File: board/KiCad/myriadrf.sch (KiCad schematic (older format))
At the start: 1 part, among them J1 FX10B_80S_8

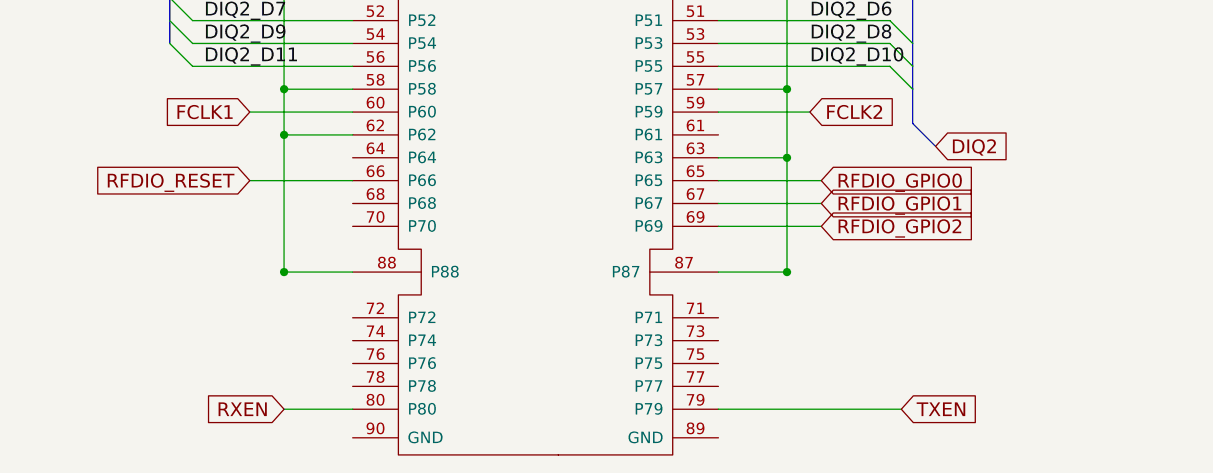
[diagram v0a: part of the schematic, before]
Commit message: control signals added
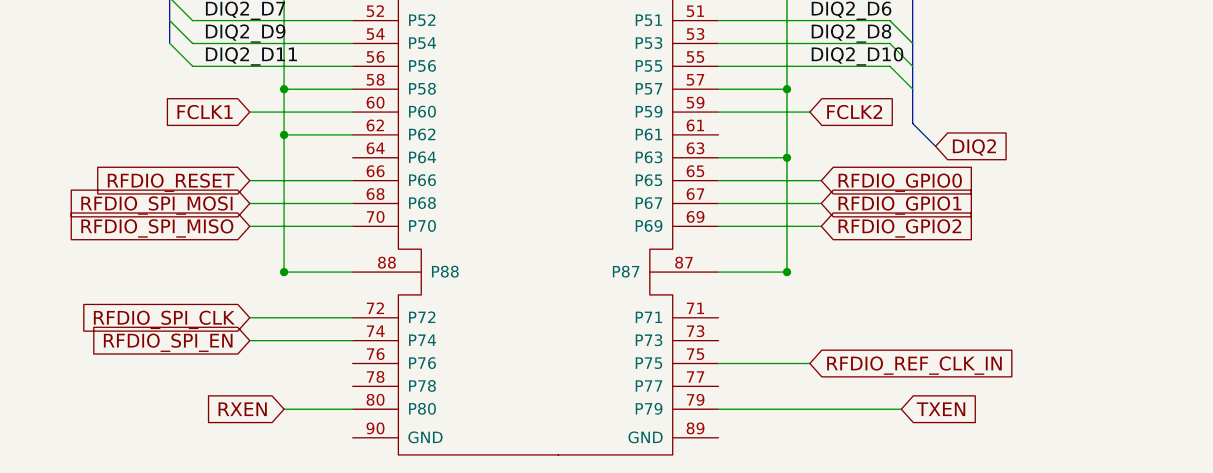
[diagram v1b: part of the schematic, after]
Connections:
- net RFDIO_SPI_MOSI: now reaches J1.68 (P68)
- net RFDIO_SPI_MISO: now reaches J1.70 (P70)
- net RFDIO_SPI_CLK: now reaches J1.72 (P72)
- net RFDIO_SPI_EN: now reaches J1.74 (P74)
- net RFDIO_REF_CLK_IN: now reaches J1.75 (P75)
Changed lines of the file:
@@
 Text GLabel 4350 5350 0    60   Input ~ 0
 RFDIO_RESET
+Wire Wire Line
+	4800 5450 4350 5450
+Text GLabel 4350 5450 0    60   Input ~ 0
+RFDIO_SPI_MOSI
+Wire Wire Line
+	4800 5550 4350 5550
+Text GLabel 4350 5550 0    60   Input ~ 0
+RFDIO_SPI_MISO
+Wire Wire Line
+	4800 5950 4350 5950
+Text GLabel 4350 5950 0    60   Input ~ 0
+RFDIO_SPI_CLK
+Wire Wire Line
+	4800 6050 4350 6050
+Text GLabel 4350 6050 0    60   Input ~ 0
+RFDIO_SPI_EN
+Wire Wire Line
+	6400 6150 6800 6150
+Text GLabel 6800 6150 2    60   Input ~ 0
+RFDIO_REF_CLK_IN
 $EndSCHEMATC

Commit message: Finalize first draft
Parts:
- J1: footprint (none) -> pmod:FX10B_80S_8
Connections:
- net GND: now also J1.89 (GND), J1.90 (GND)
- no-connect marks 0 -> 21
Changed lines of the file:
@@
 F 0 "J1" H 5600 6687 60  0000 C CNN
 F 1 "FX10B_80S_8" H 5580 6720 60  0001 C CNN
-F 2 "" H 5590 6840 60  0001 C CNN
+F 2 "pmod:FX10B_80S_8" H 5590 6840 60  0001 C CNN
 F 3 "" H 5600 3750 60  0000 C CNN
 F 4 "CONN RECEPT, 80POS, W/O, POST, SMD," H 5630 6950 60  0001 C CNN "Description"
@@
 5V
 $Comp
-L GND #PWR12
+L GND #PWR13
 U 1 1 56AB8EA2
 P 4400 1450
-F 0 "#PWR12" H 4400 1200 50  0001 C CNN
+F 0 "#PWR13" H 4400 1200 50  0001 C CNN
 F 1 "GND" H 4400 1300 50  0000 C CNN
 F 2 "" H 4400 1450 60  0000 C CNN
@@
 $EndComp
 $Comp
-L GND #PWR13
+L GND #PWR28
 U 1 1 56AB8EB8
 P 7350 1450
-F 0 "#PWR13" H 7350 1200 50  0001 C CNN
+F 0 "#PWR28" H 7350 1200 50  0001 C CNN
 F 1 "GND" H 7350 1300 50  0000 C CNN
 F 2 "" H 7350 1450 60  0000 C CNN
@@
 	1    0    0    -1
 $EndComp
-Entry Wire Line
-	7150 2650 7250 2750
-Entry Wire Line
-	7150 2750 7250 2850
-Entry Wire Line
-	7150 2950 7250 3050
-Entry Wire Line
-	7150 3350 7250 3450
-Entry Wire Line
-	7150 3450 7250 3550
-Entry Wire Line
-	7150 3550 7250 3650
 Wire Wire Line
 	6400 1250 7250 1250
@@
 Wire Wire Line
 	4800 3550 4100 3550
-Wire Bus Line
-	7250 2750 7250 3800
-Entry Wire Line
-	4000 2550 4100 2650
-Entry Wire Line
-	4000 2650 4100 2750
-Entry Wire Line
-	4000 2850 4100 2950
-Entry Wire Line
-	4000 3250 4100 3350
-Entry Wire Line
-	4000 3350 4100 3450
-Entry Wire Line
-	4000 3450 4100 3550
-Wire Bus Line
-	4000 3450 4000 2400
-Text Label 6800 2650 0    60   ~ 0
-DIQ1_D0
-Text Label 6800 2750 0    60   ~ 0
-DIQ1_D2
-Text Label 6800 2950 0    60   ~ 0
-DIQ1_D4
-Text Label 6800 3350 0    60   ~ 0
-DIQ1_D6
-Text Label 6800 3450 0    60   ~ 0
-DIQ1_D8
-Text Label 6800 3550 0    60   ~ 0
-DIQ1_D10
-Text Label 4150 2650 0    60   ~ 0
-DIQ1_D1
-Text Label 4150 2750 0    60   ~ 0
-DIQ1_D3
-Text Label 4150 2950 0    60   ~ 0
-DIQ1_D5
-Text Label 4150 3350 0    60   ~ 0
-DIQ1_D7
-Text Label 4150 3450 0    60   ~ 0
-DIQ1_D9
-Text Label 4150 3550 0    60   ~ 0
-DIQ1_D11
-Text GLabel 7350 3900 2    60   Input ~ 0
-DIQ1
-Text GLabel 3900 2300 0    60   Input ~ 0
-DIQ1
-Entry Bus Bus
-	7250 3800 7350 3900
-Entry Bus Bus
-	3900 2300 4000 2400
 Wire Wire Line
 	6400 2450 7150 2450
@@
 Text GLabel 7200 6350 2    60   Input ~ 0
 TXEN
-Wire Bus Line
-	7250 4050 7250 5100
 Wire Wire Line
 	6400 3950 7150 3950
-Entry Wire Line
-	7150 3950 7250 4050
-Entry Wire Line
-	7150 4050 7250 4150
-Entry Wire Line
-	7150 4250 7250 4350
 Wire Wire Line
 	6400 4050 7150 4050
@@
 Wire Wire Line
 	6400 4850 7150 4850
-Entry Wire Line
-	7150 4650 7250 4750
-Entry Wire Line
-	7150 4750 7250 4850
-Entry Wire Line
-	7150 4850 7250 4950
-Text Label 6800 3950 0    60   ~ 0
-DIQ2_D0
-Text Label 6800 4050 0    60   ~ 0
-DIQ2_D2
-Text Label 6800 4250 0    60   ~ 0
-DIQ2_D4
-Text Label 6800 4650 0    60   ~ 0
-DIQ2_D6
-Text Label 6800 4750 0    60   ~ 0
-DIQ2_D8
-Text Label 6800 4850 0    60   ~ 0
-DIQ2_D10
-Entry Bus Bus
-	7250 5100 7350 5200
-Text GLabel 7350 5200 2    60   Input ~ 0
-DIQ2
 Wire Wire Line
 	4800 3950 4100 3950
@@
 Wire Wire Line
 	4800 4850 4100 4850
-Entry Wire Line
-	4000 3850 4100 3950
-Entry Wire Line
-	4000 3950 4100 4050
-Entry Wire Line
-	4000 4150 4100 4250
-Entry Wire Line
-	4000 4550 4100 4650
-Entry Wire Line
-	4000 4650 4100 4750
-Entry Wire Line
-	4000 4750 4100 4850
-Wire Bus Line
-	4000 4750 4000 3850
-Entry Bus Bus
-	3900 3750 4000 3850
-Text GLabel 3900 3750 0    60   Input ~ 0
-DIQ2
-Text Label 4150 3950 0    60   ~ 0
-DIQ2_D1
-Text Label 4150 4050 0    60   ~ 0
-DIQ2_D3
-Text Label 4150 4250 0    60   ~ 0
-DIQ2_D5
-Text Label 4150 4650 0    60   ~ 0
-DIQ2_D7
-Text Label 4150 4750 0    60   ~ 0
-DIQ2_D9
-Text Label 4150 4850 0    60   ~ 0
-DIQ2_D11
 Wire Wire Line
 	6400 5050 6800 5050
@@
 Text GLabel 6800 6150 2    60   Input ~ 0
 RFDIO_REF_CLK_IN
+Text GLabel 4100 2650 0    60   Input ~ 0
+DIQ1_D1
+Text GLabel 4100 2750 0    60   Input ~ 0
+DIQ1_D3
+Text GLabel 4100 2950 0    60   Input ~ 0
+DIQ1_D5
+Text GLabel 4100 3350 0    60   Input ~ 0
+DIQ1_D7
+Text GLabel 4100 3450 0    60   Input ~ 0
+DIQ1_D9
+Text GLabel 4100 3550 0    60   Input ~ 0
+DIQ1_D11
+Text GLabel 7150 2650 2    60   Input ~ 0
+DIQ1_D0
+Text GLabel 7150 2750 2    60   Input ~ 0
+DIQ1_D2
+Text GLabel 7150 2950 2    60   Input ~ 0
+DIQ1_D4
+Text GLabel 7150 3350 2    60   Input ~ 0
+DIQ1_D6
+Text GLabel 7150 3450 2    60   Input ~ 0
+DIQ1_D8
+Text GLabel 7150 3550 2    60   Input ~ 0
+DIQ1_D10
+Text GLabel 7150 3950 2    60   Input ~ 0
+DIQ2_D0
+Text GLabel 7150 4050 2    60   Input ~ 0
+DIQ2_D2
+Text GLabel 7150 4250 2    60   Input ~ 0
+DIQ2_D4
+Text GLabel 7150 4650 2    60   Input ~ 0
+DIQ2_D6
+Text GLabel 7150 4750 2    60   Input ~ 0
+DIQ2_D8
+Text GLabel 7150 4850 2    60   Input ~ 0
+DIQ2_D10
+Text GLabel 4100 3950 0    60   Input ~ 0
+DIQ2_D1
+Text GLabel 4100 4050 0    60   Input ~ 0
+DIQ2_D3
+Text GLabel 4100 4250 0    60   Input ~ 0
+DIQ2_D5
+Text GLabel 4100 4650 0    60   Input ~ 0
+DIQ2_D7
+Text GLabel 4100 4750 0    60   Input ~ 0
+DIQ2_D9
+Text GLabel 4100 4850 0    60   Input ~ 0
+DIQ2_D11
+NoConn ~ 6400 2150
+NoConn ~ 6400 2250
+NoConn ~ 6400 2550
+NoConn ~ 6400 1650
+NoConn ~ 6400 1550
+NoConn ~ 4800 1650
+NoConn ~ 4800 1550
+NoConn ~ 4800 2150
+NoConn ~ 4800 2250
+NoConn ~ 4800 2450
+NoConn ~ 4800 2550
+NoConn ~ 4800 3750
+NoConn ~ 4800 3850
+NoConn ~ 4800 5250
+NoConn ~ 4800 6150
+NoConn ~ 4800 6250
+NoConn ~ 6400 6250
+NoConn ~ 6400 6050
+NoConn ~ 6400 5950
+NoConn ~ 6400 5150
+NoConn ~ 6400 3850
+Wire Wire Line
+	4775 6475 4800 6475
+Wire Wire Line
+	4775 6475 4775 6650
+Wire Wire Line
+	4775 6650 6425 6650
+Wire Wire Line
+	6425 6650 6425 6475
+Wire Wire Line
+	6425 6475 6400 6475
+$Comp
+L GND #PWR23
+U 1 1 56C33F19
+P 5600 6700
+F 0 "#PWR23" H 5600 6450 50  0001 C CNN
+F 1 "GND" H 5608 6526 50  0000 C CNN
+F 2 "" H 5600 6700 50  0000 C CNN
+F 3 "" H 5600 6700 50  0000 C CNN
+	1    5600 6700
+	1    0    0    -1
+$EndComp
+Wire Wire Line
+	5600 6700 5600 6650
+Connection ~ 5600 6650
 $EndSCHEMATC

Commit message: Improve design
* PMOS on input voltage for polarity
* Re-design board to add mount holes and better routing
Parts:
- added P3, P4: Myriad_Mount_Hole, pmod:Myriad_Mount_Hole, symbol Myriad_Mount_Hole
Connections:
- wire segments 77 -> 80
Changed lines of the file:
@@
 5V
 $Comp
-L GND #PWR13
+L GND #PWR26
 U 1 1 56AB8EA2
 P 4400 1450
-F 0 "#PWR13" H 4400 1200 50  0001 C CNN
+F 0 "#PWR26" H 4400 1200 50  0001 C CNN
 F 1 "GND" H 4400 1300 50  0000 C CNN
 F 2 "" H 4400 1450 60  0000 C CNN
@@
 Connection ~ 6700 2050
 Connection ~ 6700 1850
-Connection ~ 7150 1250
 Wire Wire Line
 	6400 2350 6700 2350
@@
 	6425 6475 6400 6475
 $Comp
-L GND #PWR23
+L GND #PWR27
 U 1 1 56C33F19
 P 5600 6700
-F 0 "#PWR23" H 5600 6450 50  0001 C CNN
+F 0 "#PWR27" H 5600 6450 50  0001 C CNN
 F 1 "GND" H 5608 6526 50  0000 C CNN
 F 2 "" H 5600 6700 50  0000 C CNN
@@
 	5600 6700 5600 6650
 Connection ~ 5600 6650
+$Comp
+L Myriad_Mount_Hole P3
+U 1 1 56C31CE7
+P 9550 1300
+F 0 "P3" H 9684 1353 60  0000 L CNN
+F 1 "Myriad_Mount_Hole" H 9684 1247 60  0000 L CNN
+F 2 "pmod:Myriad_Mount_Hole" H 9550 1300 60  0001 C CNN
+F 3 "" H 9550 1300 60  0000 C CNN
+	1    9550 1300
+	1    0    0    -1
+$EndComp
+$Comp
+L Myriad_Mount_Hole P4
+U 1 1 56C31DC9
+P 9550 1575
+F 0 "P4" H 9684 1628 60  0000 L CNN
+F 1 "Myriad_Mount_Hole" H 9684 1522 60  0000 L CNN
+F 2 "pmod:Myriad_Mount_Hole" H 9550 1575 60  0001 C CNN
+F 3 "" H 9550 1575 60  0000 C CNN
+	1    9550 1575
+	1    0    0    -1
+$EndComp
+Wire Wire Line
+	9125 1300 9125 1675
+Wire Wire Line
+	9125 1300 9250 1300
+Wire Wire Line
+	9250 1575 9125 1575
+Connection ~ 9125 1575
+$Comp
+L GND #PWR29
+U 1 1 56C3306B
+P 9125 1675
+F 0 "#PWR29" H 9125 1425 50  0001 C CNN
+F 1 "GND" H 9125 1525 50  0000 C CNN
+F 2 "" H 9125 1675 60  0000 C CNN
+F 3 "" H 9125 1675 60  0000 C CNN
+	1    9125 1675
+	1    0    0    -1
+$EndComp
 $EndSCHEMATC

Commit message: Housekeeping
Structure libraries and put proper licenses to them.
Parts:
- J1: footprint pmod:FX10B_80S_8 -> MyriadRF:FX10B_80S_8
- P3, P4: footprint pmod:Myriad_Mount_Hole -> lms6002-pmod:Myriad_Mount_Hole
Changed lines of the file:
@@
 LIBS:contrib
 LIBS:valves
+LIBS:lms6002-pmod
 LIBS:ice40_1k4k_tq144
 LIBS:myriad
-LIBS:pmod
-LIBS:LMS6002-Pmod-cache
 EELAYER 25 0
 EELAYER END
@@
 F 0 "J1" H 5600 6687 60  0000 C CNN
 F 1 "FX10B_80S_8" H 5580 6720 60  0001 C CNN
-F 2 "pmod:FX10B_80S_8" H 5590 6840 60  0001 C CNN
+F 2 "MyriadRF:FX10B_80S_8" H 5590 6840 60  0001 C CNN
 F 3 "" H 5600 3750 60  0000 C CNN
 F 4 "CONN RECEPT, 80POS, W/O, POST, SMD," H 5630 6950 60  0001 C CNN "Description"
@@
 F 0 "P3" H 9684 1353 60  0000 L CNN
 F 1 "Myriad_Mount_Hole" H 9684 1247 60  0000 L CNN
-F 2 "pmod:Myriad_Mount_Hole" H 9550 1300 60  0001 C CNN
+F 2 "lms6002-pmod:Myriad_Mount_Hole" H 9550 1300 60  0001 C CNN
 F 3 "" H 9550 1300 60  0000 C CNN
 	1    9550 1300
@@
 F 0 "P4" H 9684 1628 60  0000 L CNN
 F 1 "Myriad_Mount_Hole" H 9684 1522 60  0000 L CNN
-F 2 "pmod:Myriad_Mount_Hole" H 9550 1575 60  0001 C CNN
+F 2 "lms6002-pmod:Myriad_Mount_Hole" H 9550 1575 60  0001 C CNN
 F 3 "" H 9550 1575 60  0000 C CNN
 	1    9550 1575
